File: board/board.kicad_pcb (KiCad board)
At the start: 4 copper layers, 21 x 13 mm, 17 parts, among them J1 022_battery_cells, J2 003_power

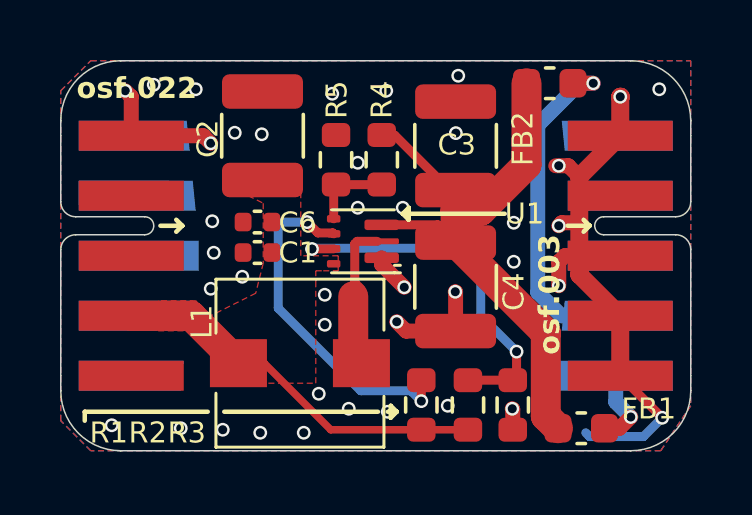
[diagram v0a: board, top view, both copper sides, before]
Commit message: reduced ground pins to be compatable with more connector types
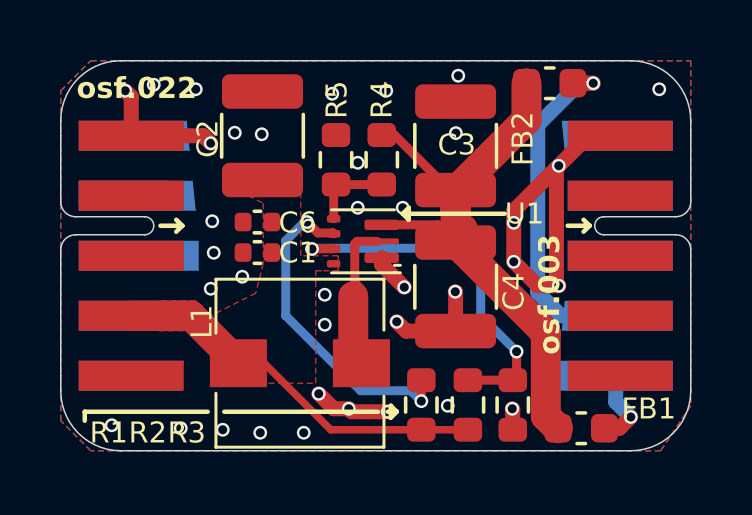
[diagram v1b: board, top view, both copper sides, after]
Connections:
- J2 pad 2: GND -> unconnected-(J2-GND-Pad2)
- J2 pad 3: GND -> unconnected-(J2-GND-Pad3)
- J2 pad 4: GND -> unconnected-(J2-GND-Pad4)
- J2 pad 5: GND -> unconnected-(J2-GND-Pad5)
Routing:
- net GND: track 29.6 -> 24.5 mm, vias 40 -> 37
- net /implementation/EN: track 11.6 -> 10.9 mm
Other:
- board text added: "b140_v1.1 step_up_converter_TPS61022"
- board text removed: "b140_v1.0 step_up_converter_TPS61022"
